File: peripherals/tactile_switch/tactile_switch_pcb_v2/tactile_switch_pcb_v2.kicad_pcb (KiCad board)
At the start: 2 copper layers, 18.8 x 34 mm, 3 parts, among them J1 PJ320A, SW1 SW_Push

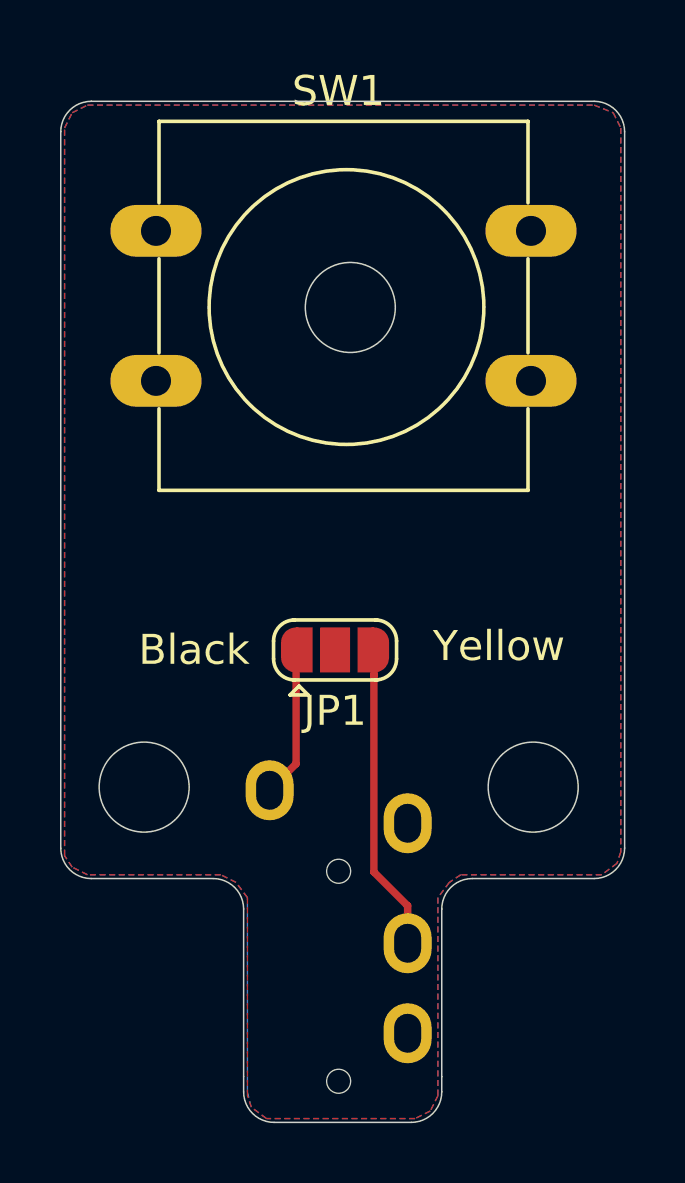
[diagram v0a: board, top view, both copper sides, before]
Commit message: Increased tactile switch PCB hole diameters   - increased hole diameters to 1.2mm to accommodate pins     on 12mm x 12mm tactile switches.
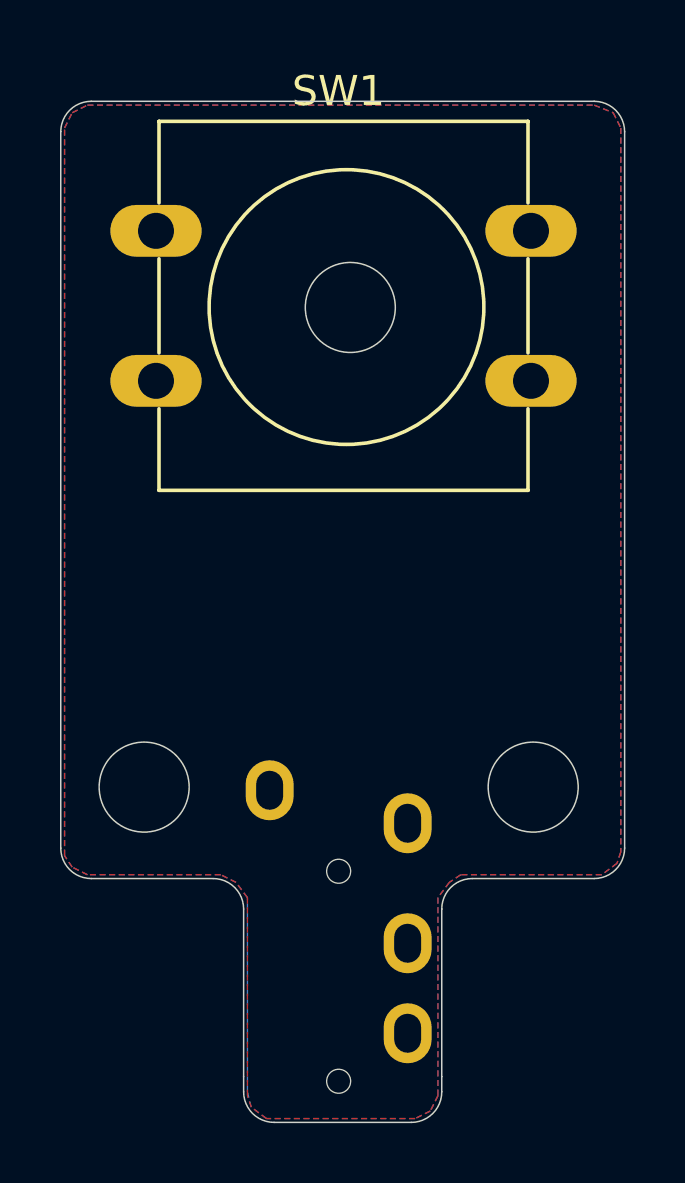
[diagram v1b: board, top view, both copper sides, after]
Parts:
- removed JP1: SolderJumper_3_Open, Jumper:SolderJumper-3_P1.3mm_Open_RoundedPad1.0x1.5mm
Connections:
- net /2 renamed /Tip
- J1 pad 2: Net-(J1-Pad2) -> (no net)
- J1 pad 3: Net-(J1-Pad3) -> /Ring1
- J1 pad 5: Net-(J1-Pad5) -> (no net)
- SW1 pad 1: /1 -> /Ring1
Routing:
- net Net-(J1-Pad3): track 10.2 -> 0.00 mm
- net Net-(J1-Pad5): track 5.04 -> 0.00 mm
- added copper zone on F.Cu, net /Ring1
- removed copper zone on F.Cu, net /1
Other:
- board text added: "Tactile Switch Interface Ver. 2.1"
- board text removed: "Black"
- board text removed: "Tactile Switch Interface Ver. 2.0"
- board text removed: "Yellow"
